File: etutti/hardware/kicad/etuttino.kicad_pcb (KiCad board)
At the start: 2 copper layers, 183.4 x 132.2 mm, 80 parts, among them J1 PinSocket_1x14_P2.54mm_Vertic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, J2 PinSocket_1x14_P2.54mm_Vertic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, SW1 Kailh_MX_Hotswap_1u, SW10 Kailh_MX_Hotswap_1u, SW11 Kailh_MX_Hotswap_1u, SW12 Kailh_MX_Hotswap_1u, SW13 Kailh_MX_Hotswap_1u, SW14 Kailh_MX_Hotswap_1u, SW15 Kailh_MX_Hotswap_1u, SW16 Kailh_MX_Hotswap_1u, SW17 Kailh_MX_Hotswap_1u, SW18 Kailh_MX_Hotswap_1u, SW19 Kailh_MX_Hotswap_1u, SW2 Kailh_MX_Hotswap_1u, SW20 Kailh_MX_Hotswap_1u, SW21 Kailh_MX_Hotswap_1u, SW22 Kailh_MX_Hotswap_1u, SW23 Kailh_MX_Hotswap_1u, SW24 Kailh_MX_Hotswap_1u, SW25 Kailh_MX_Hotswap_1u, SW26 Kailh_MX_Hotswap_1u, SW27 Kailh_MX_Hotswap_1u, SW28 Kailh_MX_Hotswap_1u, SW29 Kailh_MX_Hotswap_1u, SW3 Kailh_MX_Hotswap_1u, SW30 Kailh_MX_Hotswap_1u, SW31 Kailh_MX_Hotswap_1u, SW32 Kailh_MX_Hotswap_1u, SW33 Kailh_MX_Hotswap_1u, SW34 Kailh_MX_Hotswap_1u, SW4 Kailh_MX_Hotswap_1u, SW5 Kailh_MX_Hotswap_1u, SW6 Kailh_MX_Hotswap_1u, SW7 Kailh_MX_Hotswap_1u, SW8 Kailh_MX_Hotswap_1u, SW9 Kailh_MX_Hotswap_1u

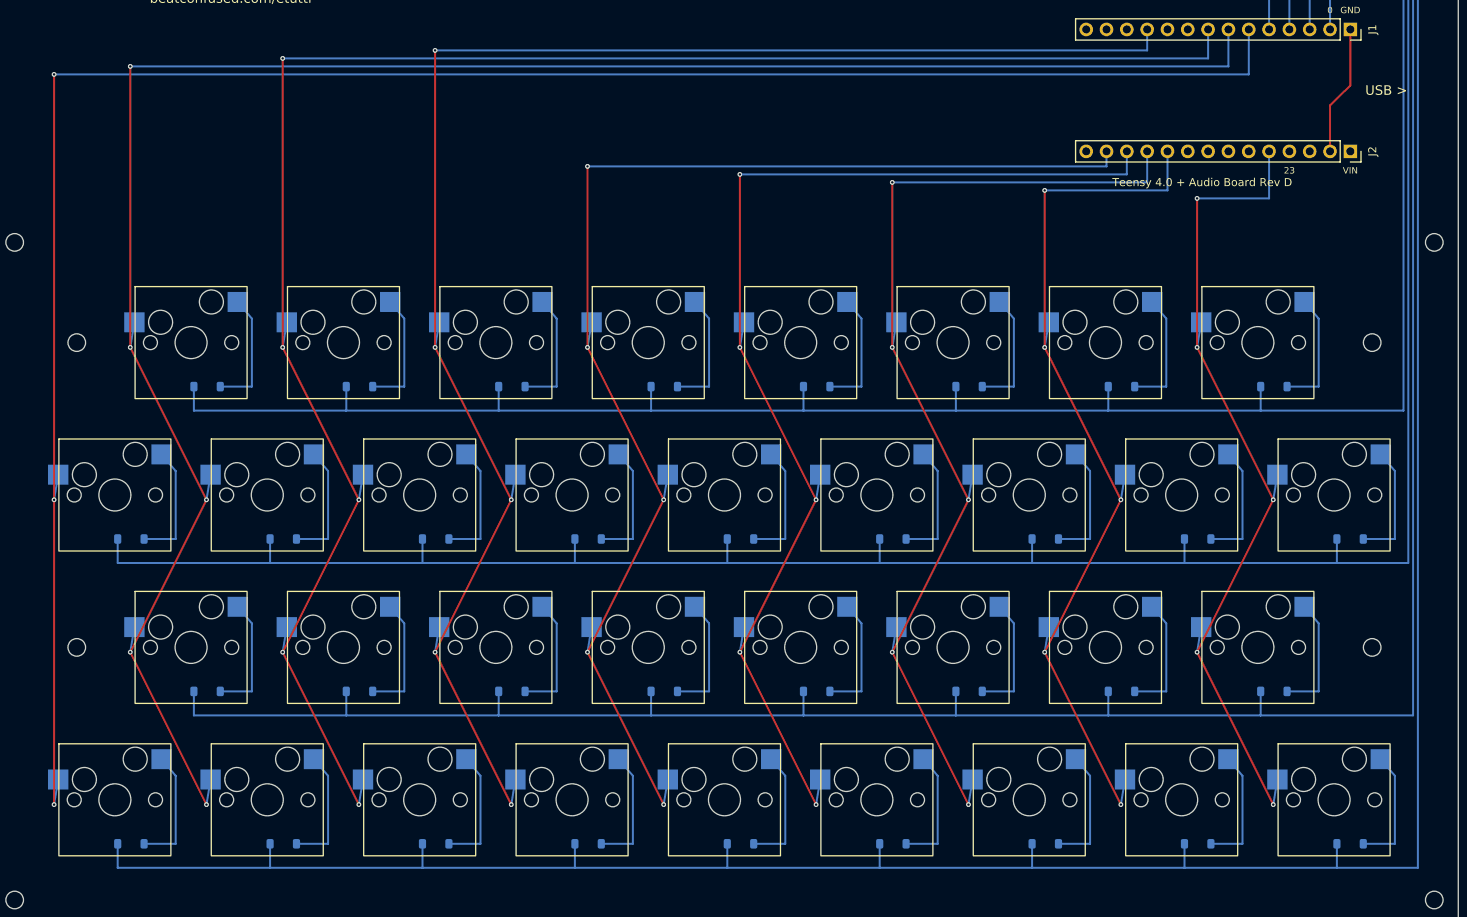
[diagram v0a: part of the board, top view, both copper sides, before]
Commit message: eTuttino: round keys, row 1 at the bottom, B-griff, presets, keyboard toggle
Page:
- Round accordion buttons (on-screen and in the model renders).
- Row 1 is now nearest the player (bottom), row 4 at the top.
- C-griff / B-griff switch (B = mirror image, rows 1 and 3 swapped);
  sent to the Teensy as CC 24 so the physical keys follow. Remembered.
- Computer-keyboard input is now a toggle (remembered) with the new
  mapping: row 1 Z..Comma, row 2 A..L, row 3 W..O, row 4 2..0 (by
  physical key, so it matches ABNT2). Key legends hide when it's off.
- Synth: instrument presets (classic accordion = default = two reeds a
  few cents apart in a soft cassotto; jazz accordion; piano; bass;
  guitar), "Reset to default", a "modified" marker, and voice 2
  controls (waveform, octave, level, detune).

Firmware: two oscillators per voice (voice 2 waveform/level/detune/
octave on CC 20-23), C/B-griff note tables switchable by CC 24 (held
keys release the note they started), row pins reordered for the flipped
PCB, defaults = the classic accordion preset. Compiled clean
(teensy40, usb=midi) and uploaded to the connected Teensy.

PCB: flipped so row 1 is at the front; router now ranks rows/columns by
height instead of row number; still DRC-clean. build_pcb.py now reads
the board back and checks every key's row/column pins against the
firmware tables (fails on mismatch; mutation-tested).

Co-Authored-By: Claude Opus 5.5 <noreply@anthropic.com>
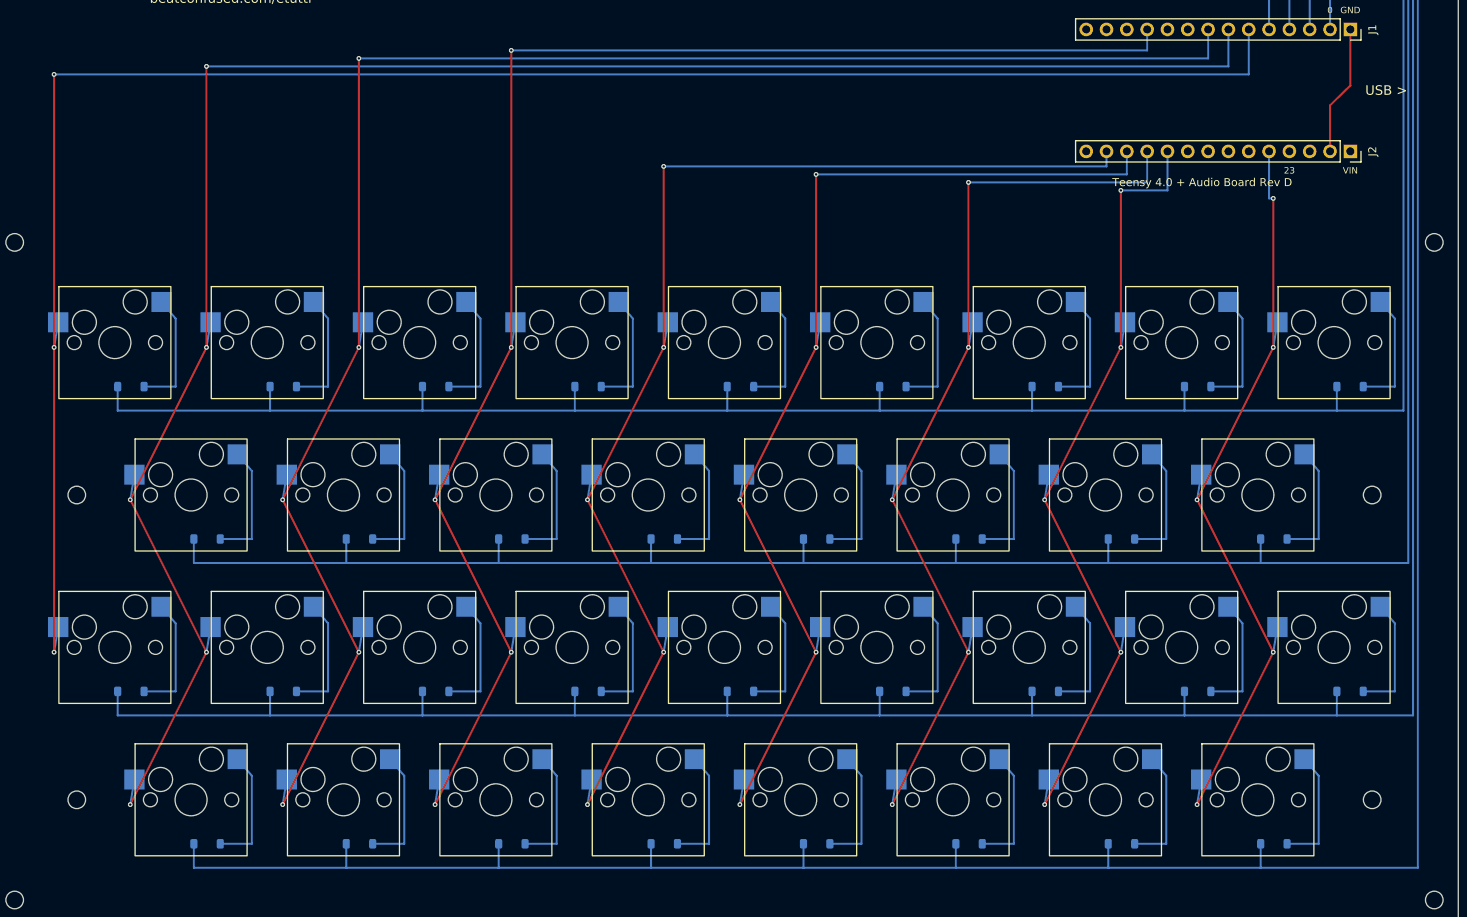
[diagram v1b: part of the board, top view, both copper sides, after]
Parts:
- moved H7 57.1 mm to (10.8, 116.7)
- moved H8 57.1 mm to (172.7, 116.7)
- moved SW1 57.1 mm to (25.1, 116.7)
- moved SW2 57.1 mm to (44.1, 116.7)
- moved SW26 57.1 mm to (15.5, 59.5)
- moved SW27 57.1 mm to (34.6, 59.5)
- moved SW28 57.1 mm to (53.6, 59.5)
- moved SW29 57.1 mm to (72.7, 59.5)
- moved SW3 57.1 mm to (63.1, 116.7)
- moved SW30 57.1 mm to (91.7, 59.5)
- moved SW31 57.1 mm to (110.8, 59.5)
- moved SW32 57.1 mm to (129.8, 59.5)
- moved SW33 57.1 mm to (148.9, 59.5)
- moved SW34 57.1 mm to (167.9, 59.5)
- moved SW4 57.1 mm to (82.2, 116.7)
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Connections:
- J1 pad 2: ROW0 -> ROW3
- J1 pad 3: ROW1 -> ROW2
- J1 pad 4: ROW2 -> ROW1
- J1 pad 5: ROW3 -> ROW0
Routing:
- net ROW0: track 240.8 -> 315.2 mm
- net ROW3: track 327.7 -> 253.3 mm
- net ROW1: track 278.1 -> 302.9 mm
- net ROW2: track 290.4 -> 265.6 mm
- net COL0: track 252.6 -> 233.5 mm
- net COL7: track 116.5 -> 107.0 mm
- net COL3: track 205.4 -> 195.9 mm
- net COL1: track 253.6 -> 244.1 mm
- net COL4: track 166.0 -> 156.5 mm
- net COL2: track 232.0 -> 222.5 mm
- net COL5: track 149.5 -> 140.0 mm
- net COL6: track 133.0 -> 123.5 mm
- net COL8: track 110.1 -> 101.7 mm

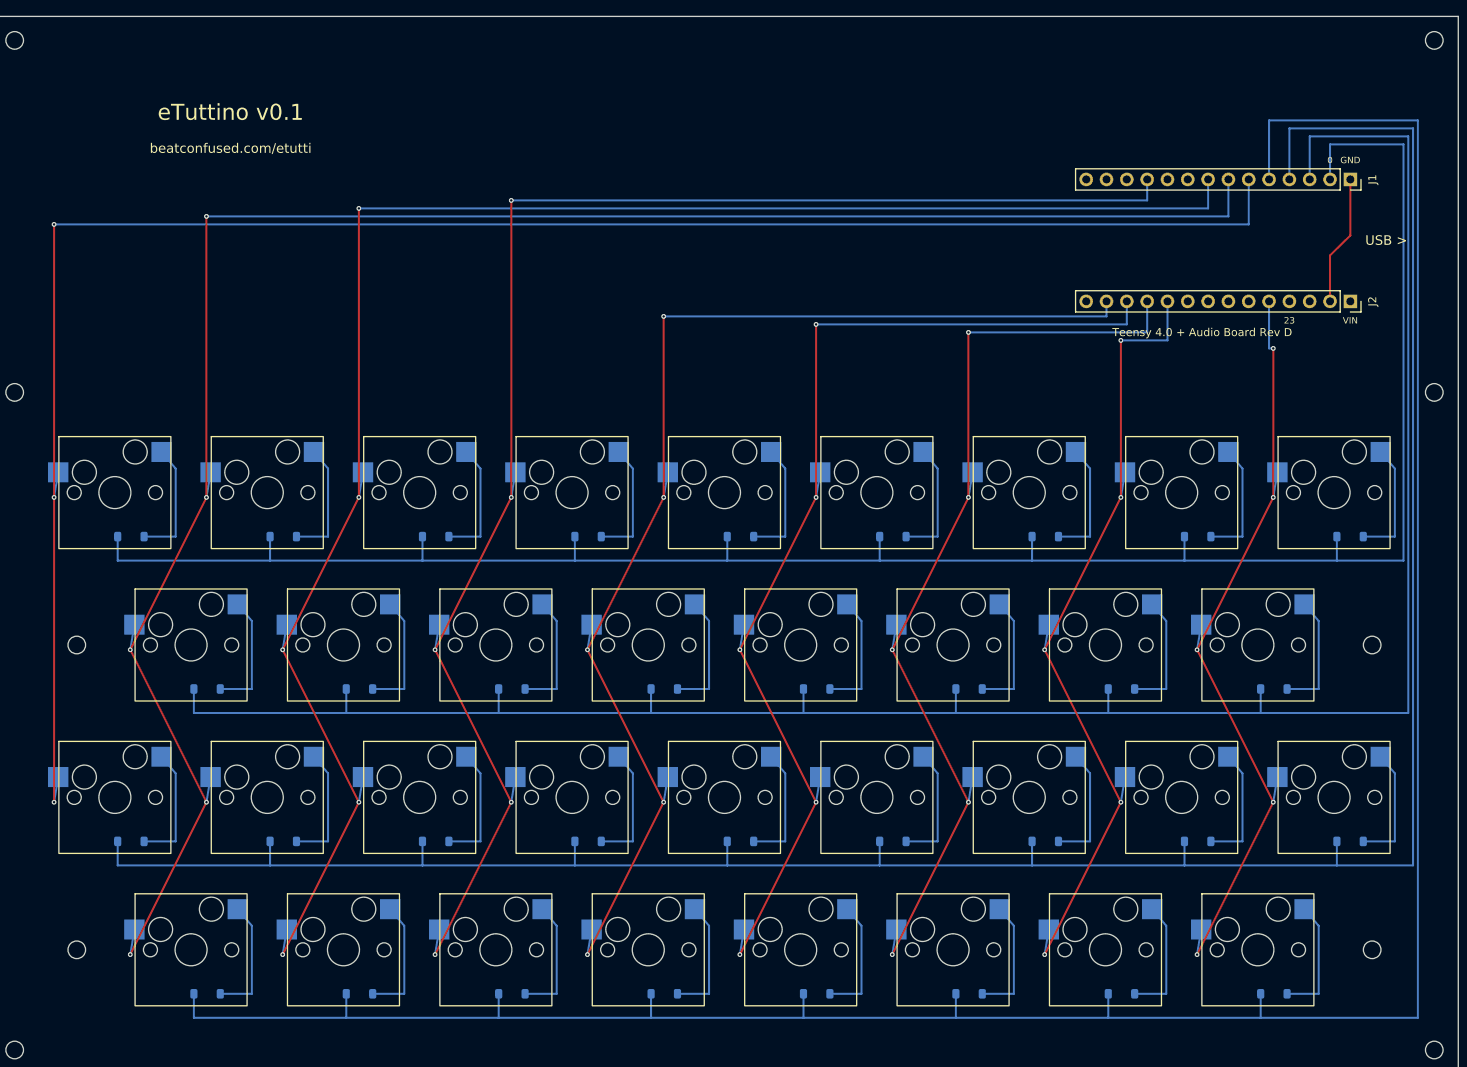
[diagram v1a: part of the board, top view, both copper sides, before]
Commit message: eTuttino: Hall-effect keys with velocity, assembly and user manuals
PCB (etutti/hardware):
- Gateron magnetic switches (no pins, plate mounted) with a DRV5056A3
  Hall sensor under each one, on the BACK of a 1.2 mm board: the DRV5056
  only reads a south pole facing its marked side and Gateron magnets are
  north-down, so the field has to come through the board from behind.
- 3 x CD74HC4067 analog muxes (address on pins 0-3, outputs to A0-A2),
  AMS1117-3.3 rail from VIN for the 34 sensors (~200 mA).
- build_pcb.py: fixed per-key wiring and power buses, then its own A*
  grid router (two layers, vias, KiCad clearances) for everything else.
  DRC 0/0/0, firmware cross-check 34/34. JLCPCB BOM/CPL for bottom-side
  assembly. generate.py owns the sensor -> mux channel map and prints the
  firmware's KEY_INPUT table.

Firmware: reads the sensors through the muxes (~240 us per full scan,
measured), cube-root travel model between per-key rest and learnt bottom
(EEPROM), velocity from the time between 12 % and 45 % of the travel.
CC 9 velocity curve, CC 14 recalibrate, CC 15 key-test stream. Pull-downs
on the mux outputs: a bare Teensy has no stray notes (verified on the
user's Teensy: 0 keys present, 0 notes).

Page: "eTuttino keys" panel (velocity curve, Calibrate, Key test rings),
link to the new etutti/manuais/ page: assembly route A (factory-soldered
via JLCPCB PCBA), route B (soldered at home), final assembly, user manual,
in en/pt/es.

Co-Authored-By: Claude Opus 5.5 <noreply@anthropic.com>
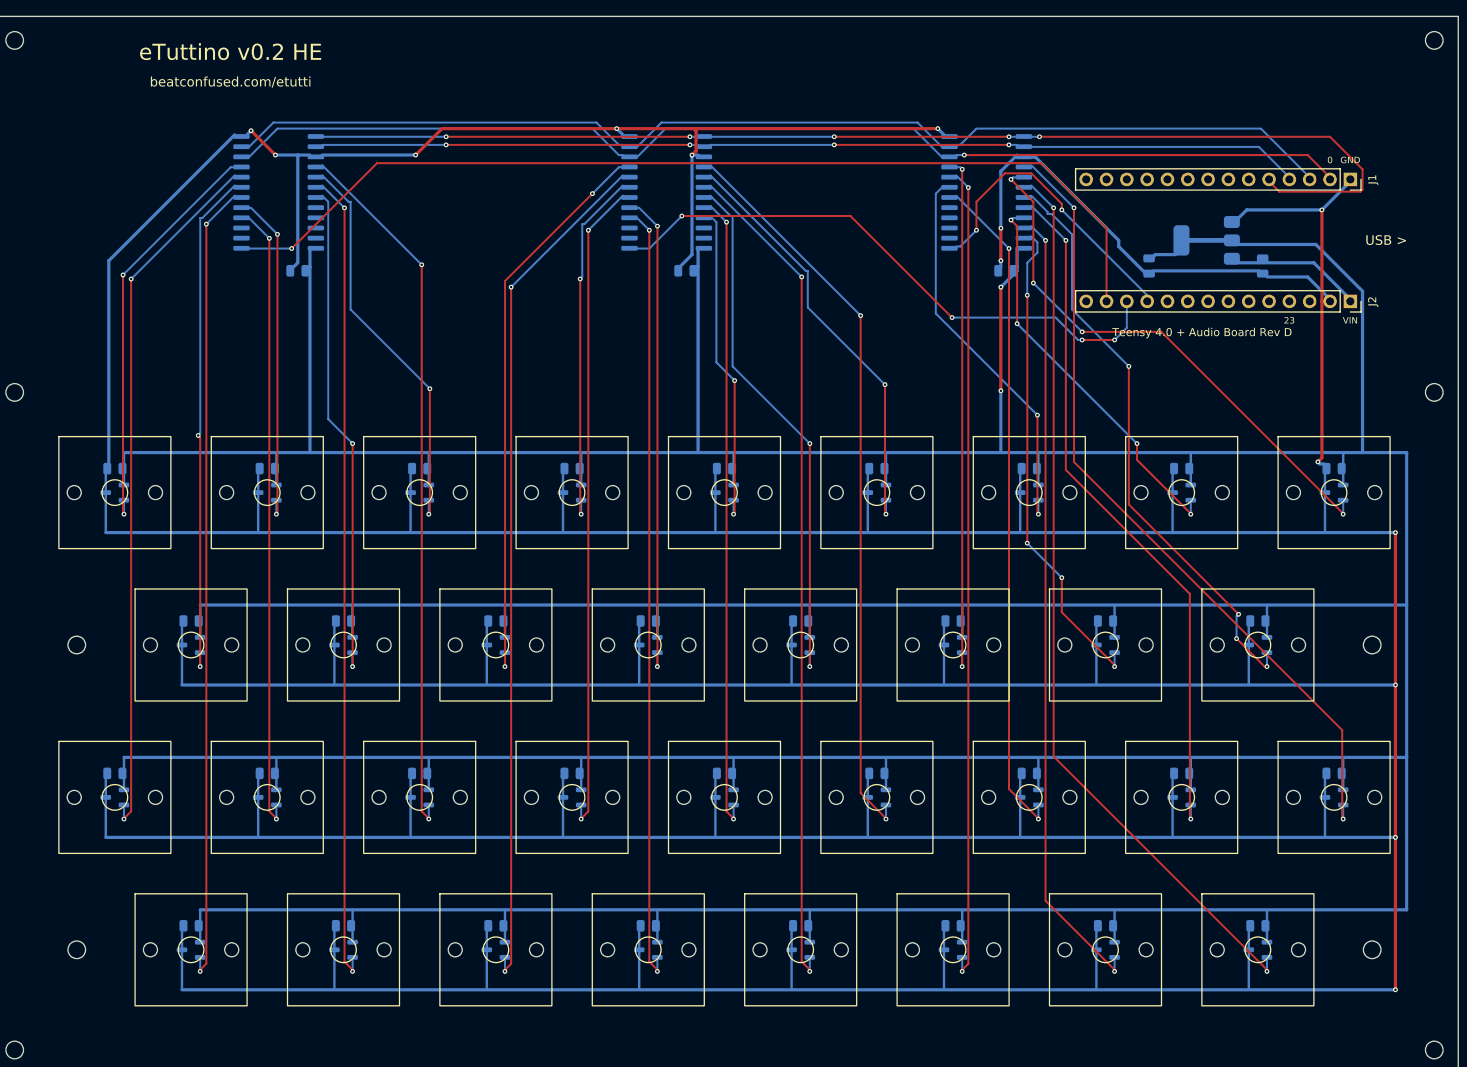
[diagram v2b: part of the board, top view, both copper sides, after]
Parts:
- removed D1, D10, D11, D12, D13, D14, D15, D16, D17, D18, D19, D2, D20, D21, D22, D23, D24, D25, D26, D27, D28, D29, D3, D30, D31, D32, D33, D34, D4, D5, D6, D7, D8, D9: D_SOD-123, D_SOD-123
- added C1: 100nF, C_0805_2012Metric, B.Cu at (25.1, 113.7)
- added C10: 100nF, C_0805_2012Metric, B.Cu at (34.6, 94.6)
- added C11: 100nF, C_0805_2012Metric, B.Cu at (53.6, 94.6)
- added C12: 100nF, C_0805_2012Metric, B.Cu at (72.7, 94.6)
- added C13: 100nF, C_0805_2012Metric, B.Cu at (91.7, 94.6)
- added C14: 100nF, C_0805_2012Metric, B.Cu at (110.8, 94.6)
- added C15: 100nF, C_0805_2012Metric, B.Cu at (129.8, 94.6)
- added C16: 100nF, C_0805_2012Metric, B.Cu at (148.9, 94.6)
- added C17: 100nF, C_0805_2012Metric, B.Cu at (167.9, 94.6)
- added C18: 100nF, C_0805_2012Metric, B.Cu at (25.1, 75.6)
- added C19: 100nF, C_0805_2012Metric, B.Cu at (44.1, 75.6)
- added C2: 100nF, C_0805_2012Metric, B.Cu at (44.1, 113.7)
- added C20: 100nF, C_0805_2012Metric, B.Cu at (63.1, 75.6)
- added C21: 100nF, C_0805_2012Metric, B.Cu at (82.2, 75.6)
- added C22: 100nF, C_0805_2012Metric, B.Cu at (101.2, 75.6)
- added C23: 100nF, C_0805_2012Metric, B.Cu at (120.3, 75.6)
- added C24: 100nF, C_0805_2012Metric, B.Cu at (139.3, 75.6)
- added C25: 100nF, C_0805_2012Metric, B.Cu at (158.4, 75.6)
- added C26: 100nF, C_0805_2012Metric, B.Cu at (15.5, 56.5)
- added C27: 100nF, C_0805_2012Metric, B.Cu at (34.6, 56.5)
- added C28: 100nF, C_0805_2012Metric, B.Cu at (53.6, 56.5)
- added C29: 100nF, C_0805_2012Metric, B.Cu at (72.7, 56.5)
- added C3: 100nF, C_0805_2012Metric, B.Cu at (63.1, 113.7)
- added C30: 100nF, C_0805_2012Metric, B.Cu at (91.7, 56.5)
- added C31: 100nF, C_0805_2012Metric, B.Cu at (110.8, 56.5)
- added C32: 100nF, C_0805_2012Metric, B.Cu at (129.8, 56.5)
- added C33: 100nF, C_0805_2012Metric, B.Cu at (148.9, 56.5)
- added C34: 100nF, C_0805_2012Metric, B.Cu at (167.9, 56.5)
- added C4: 100nF, C_0805_2012Metric, B.Cu at (82.2, 113.7)
- added C41: 100nF, C_0805_2012Metric, B.Cu at (38.4, 31.8)
- added C42: 100nF, C_0805_2012Metric, B.Cu at (86.9, 31.8)
- added C43: 100nF, C_0805_2012Metric, B.Cu at (126.9, 31.8)
- added C5: 100nF, C_0805_2012Metric, B.Cu at (101.2, 113.7)
- added C50: 10uF, C_0805_2012Metric, B.Cu at (159.0, 31.2)
- added C51: 22uF, C_0805_2012Metric, B.Cu at (144.8, 31.2)
- added C6: 100nF, C_0805_2012Metric, B.Cu at (120.3, 113.7)
- added C7: 100nF, C_0805_2012Metric, B.Cu at (139.3, 113.7)
- added C8: 100nF, C_0805_2012Metric, B.Cu at (158.4, 113.7)
- added C9: 100nF, C_0805_2012Metric, B.Cu at (15.5, 94.6)
- added U1: DRV5056A3QDBZR, SOT-23-3, B.Cu at (25.1, 116.7)
- added U10: DRV5056A3QDBZR, SOT-23-3, B.Cu at (34.6, 97.6)
- added U11: DRV5056A3QDBZR, SOT-23-3, B.Cu at (53.6, 97.6)
- added U12: DRV5056A3QDBZR, SOT-23-3, B.Cu at (72.7, 97.6)
- added U13: DRV5056A3QDBZR, SOT-23-3, B.Cu at (91.7, 97.6)
- added U14: DRV5056A3QDBZR, SOT-23-3, B.Cu at (110.8, 97.6)
- added U15: DRV5056A3QDBZR, SOT-23-3, B.Cu at (129.8, 97.6)
- added U16: DRV5056A3QDBZR, SOT-23-3, B.Cu at (148.9, 97.6)
- added U17: DRV5056A3QDBZR, SOT-23-3, B.Cu at (167.9, 97.6)
- added U18: DRV5056A3QDBZR, SOT-23-3, B.Cu at (25.1, 78.6)
- added U19: DRV5056A3QDBZR, SOT-23-3, B.Cu at (44.1, 78.6)
- added U2: DRV5056A3QDBZR, SOT-23-3, B.Cu at (44.1, 116.7)
- added U20: DRV5056A3QDBZR, SOT-23-3, B.Cu at (63.1, 78.6)
- added U21: DRV5056A3QDBZR, SOT-23-3, B.Cu at (82.2, 78.6)
- added U22: DRV5056A3QDBZR, SOT-23-3, B.Cu at (101.2, 78.6)
- added U23: DRV5056A3QDBZR, SOT-23-3, B.Cu at (120.3, 78.6)
- added U24: DRV5056A3QDBZR, SOT-23-3, B.Cu at (139.3, 78.6)
- added U25: DRV5056A3QDBZR, SOT-23-3, B.Cu at (158.4, 78.6)
- added U26: DRV5056A3QDBZR, SOT-23-3, B.Cu at (15.5, 59.5)
- added U27: DRV5056A3QDBZR, SOT-23-3, B.Cu at (34.6, 59.5)
- added U28: DRV5056A3QDBZR, SOT-23-3, B.Cu at (53.6, 59.5)
- added U29: DRV5056A3QDBZR, SOT-23-3, B.Cu at (72.7, 59.5)
- added U3: DRV5056A3QDBZR, SOT-23-3, B.Cu at (63.1, 116.7)
- added U30: DRV5056A3QDBZR, SOT-23-3, B.Cu at (91.7, 59.5)
- added U31: DRV5056A3QDBZR, SOT-23-3, B.Cu at (110.8, 59.5)
- added U32: DRV5056A3QDBZR, SOT-23-3, B.Cu at (129.8, 59.5)
- added U33: DRV5056A3QDBZR, SOT-23-3, B.Cu at (148.9, 59.5)
- added U34: DRV5056A3QDBZR, SOT-23-3, B.Cu at (167.9, 59.5)
- added U4: DRV5056A3QDBZR, SOT-23-3, B.Cu at (82.2, 116.7)
- added U41: CD74HC4067M96, SOIC-24W_7.5x15.4mm_P1.27mm, B.Cu at (36.0, 22.0)
- added U42: CD74HC4067M96, SOIC-24W_7.5x15.4mm_P1.27mm, B.Cu at (84.5, 22.0)
- added U43: CD74HC4067M96, SOIC-24W_7.5x15.4mm_P1.27mm, B.Cu at (124.5, 22.0)
- added U5: DRV5056A3QDBZR, SOT-23-3, B.Cu at (101.2, 116.7)
- added U50: AMS1117-3.3, SOT-223-3_TabPin2, B.Cu at (152.0, 28.0)
- added U6: DRV5056A3QDBZR, SOT-23-3, B.Cu at (120.3, 116.7)
- added U7: DRV5056A3QDBZR, SOT-23-3, B.Cu at (139.3, 116.7)
- added U8: DRV5056A3QDBZR, SOT-23-3, B.Cu at (158.4, 116.7)
- added U9: DRV5056A3QDBZR, SOT-23-3, B.Cu at (15.5, 97.6)
- SW1, SW10, SW11, SW12, SW13, SW14, SW15, SW16, SW17, SW18, SW19, SW2, SW20, SW21, SW22, SW23, SW24, SW25, SW26, SW27, SW28, SW29, SW3, SW30, SW31, SW32, SW33, SW34, SW4, SW5, SW6, SW7, SW8, SW9: value Kailh_MX_Hotswap_1u -> Gateron_Magnetic_MX_1u; footprint Kailh_MX_Hotswap_1u -> Gateron_Magnetic_MX_1u
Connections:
- J1 pad 11: COL3 -> (no net)
- J1 pad 2: ROW3 -> SEL0
- J1 pad 3: ROW2 -> SEL1
- J1 pad 4: ROW1 -> SEL2
- J1 pad 5: ROW0 -> SEL3
- J1 pad 6: COL0 -> (no net)
- J1 pad 7: COL1 -> (no net)
- J1 pad 8: COL2 -> (no net)
- J2 pad 1: (no net) -> VIN
- J2 pad 10: COL7 -> (no net)
- J2 pad 11: COL6 -> COM2
- J2 pad 12: COL5 -> COM1
- J2 pad 13: COL4 -> COM0
- J2 pad 5: COL8 -> (no net)
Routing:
- net GND: track 16.3 -> 1230.9 mm, vias 0 -> 14
- net VCC: track 0.00 -> 942.6 mm, vias 0 -> 2
- net ROW0: track 315.2 -> 0.00 mm
- net ROW1: track 302.9 -> 0.00 mm
- net ROW2: track 265.6 -> 0.00 mm
- net ROW3: track 253.3 -> 0.00 mm
- net COL1: track 244.1 -> 0.00 mm, vias 5 -> 0
- net COL0: track 233.5 -> 0.00 mm, vias 3 -> 0
- net COL2: track 222.5 -> 0.00 mm, vias 5 -> 0
- net COL3: track 195.9 -> 0.00 mm, vias 5 -> 0
- net COL4: track 156.5 -> 0.00 mm, vias 5 -> 0
- net SEL3: track 0.00 -> 142.9 mm, vias 0 -> 5
- net COL5: track 140.0 -> 0.00 mm, vias 5 -> 0
- net SEL0: track 0.00 -> 138.2 mm, vias 0 -> 1
- net SEL1: track 0.00 -> 137.0 mm
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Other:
- board text added: "Sensors DRV5056A3, back side, under each switch"
- board text added: "eTuttino v0.2 HE"
- board text added: "eTuttino v0.2 HE - C-griff G3-G5"
- board text removed: "eTuttino v0.1"
- board text removed: "eTuttino v0.1 - C-griff G3-G5"
